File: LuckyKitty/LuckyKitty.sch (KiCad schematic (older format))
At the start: 19 parts

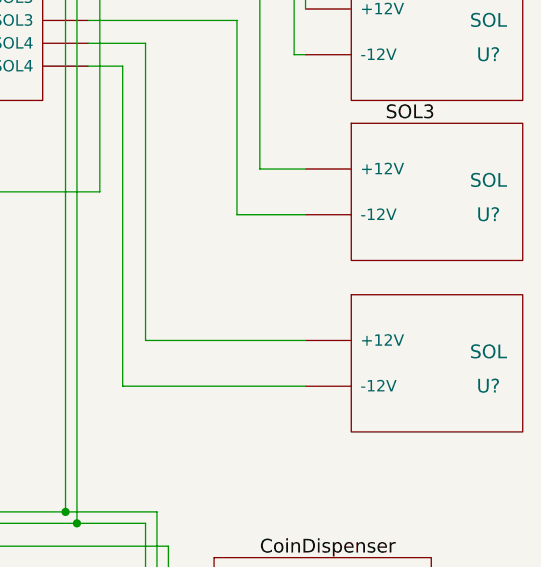
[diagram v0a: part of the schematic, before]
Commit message: Fixes a missing label on SOL4
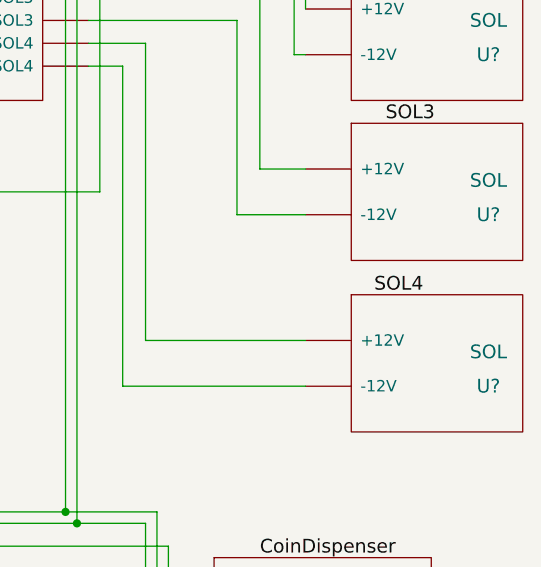
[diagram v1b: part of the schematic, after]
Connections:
- net at U?.~ (Vin): now also U?.~ (GND)
- net at U?.~ (SOL4): now also U?.~ (-12V); no longer U?.~ (-12V)
- new net: U?.~ (-12V), U?.~ (GND), U?.~ (Lin), U?.~ (SOL4)
- new net: U?.~ (GND), U?.~ (Lin), U?.~ (SOL4)
- new net: U?.~ (Din), U?.~ (Din), U?.~ (GND), U?.~ (GND), U?.~ (Lin), U?.~ (MOSI), U?.~ (MOSI), U?.~ (MOSI), U?.~ (SOL4), U?.~ (Vin)
- new net: U?.~ (Din), U?.~ (Din), U?.~ (Din), U?.~ (GND), U?.~ (MOSI), U?.~ (MOSI), U?.~ (MOSI), U?.~ (SOL4), U?.~ (Vin)
- new net: U?.0 (MOSI1), U?.~ (MOSI), U?.~ (MOSI), U?.~ (MOSI)
- new net: U?.1 (MISO1), U?.~ (MOSI), U?.~ (MOSI), U?.~ (MOSI)
- new net: U?.24, U?.~ (MOSI), U?.~ (MOSI), U?.~ (MOSI)
- new net: U?.32 (SCK1), U?.~ (MOSI), U?.~ (MOSI), U?.~ (MOSI)
- new net: U?.~ (Lin), U?.~ (Vin)
- new net: U?.~ (-12V), U?.~ (SOL4) (x4)
- now unconnected: U?.~ (-12V), U?.~ (Din), U?.~ (MOSI), U?.~ (MOSI), U?.~ (MOSI), U?.~ (MOSI), U?.~ (MOSI), U?.~ (MOSI), U?.~ (MOSI), U?.~ (MOSI), U?.~ (MOSI), U?.~ (MOSI), U?.~ (MOSI), U?.~ (MOSI), U?.~ (MOSI), U?.~ (MOSI), U?.~ (MOSI), U?.~ (MOSI), U?.~ (MOSI), U?.~ (MOSI)
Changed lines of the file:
@@
 LIBS:adafruit
 LIBS:Custom
+LIBS:LuckyKitty-cache
 EELAYER 25 0
 EELAYER END
@@
 Text Label 2750 650  0    60   ~ 0
 Examine
+Text Label 10350 4400 0    60   ~ 0
+SOL4
 $EndSCHEMATC

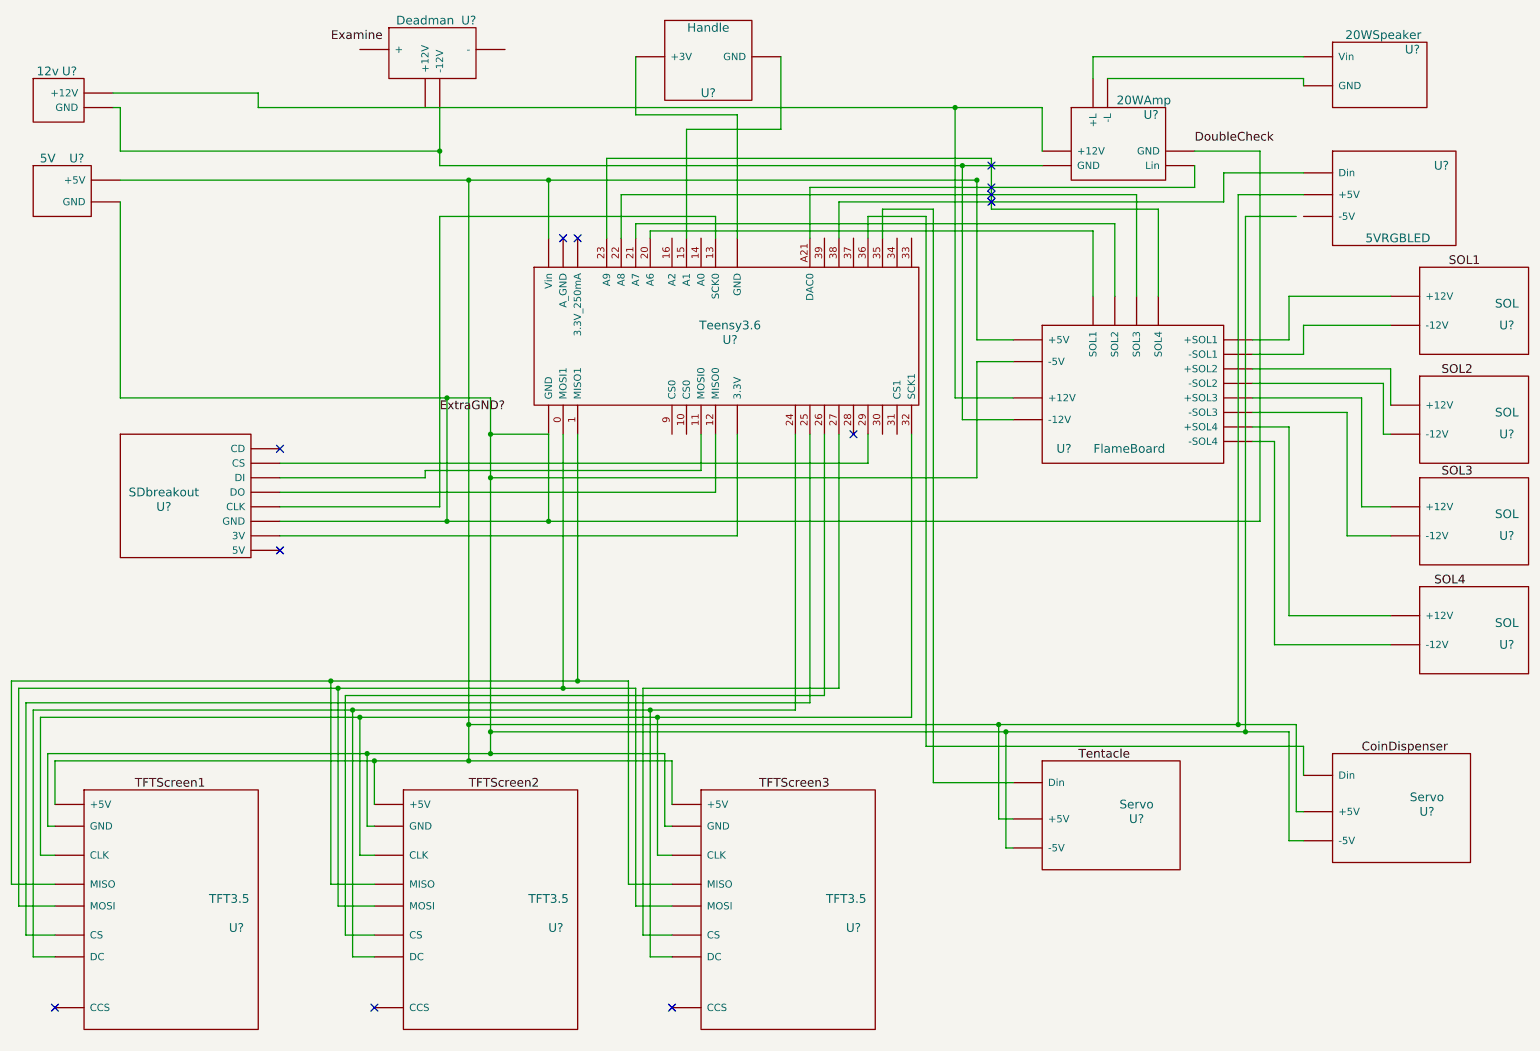
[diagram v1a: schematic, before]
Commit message: Adds safety lighting, fixes handle and sd breakout 5v, adds deadman init
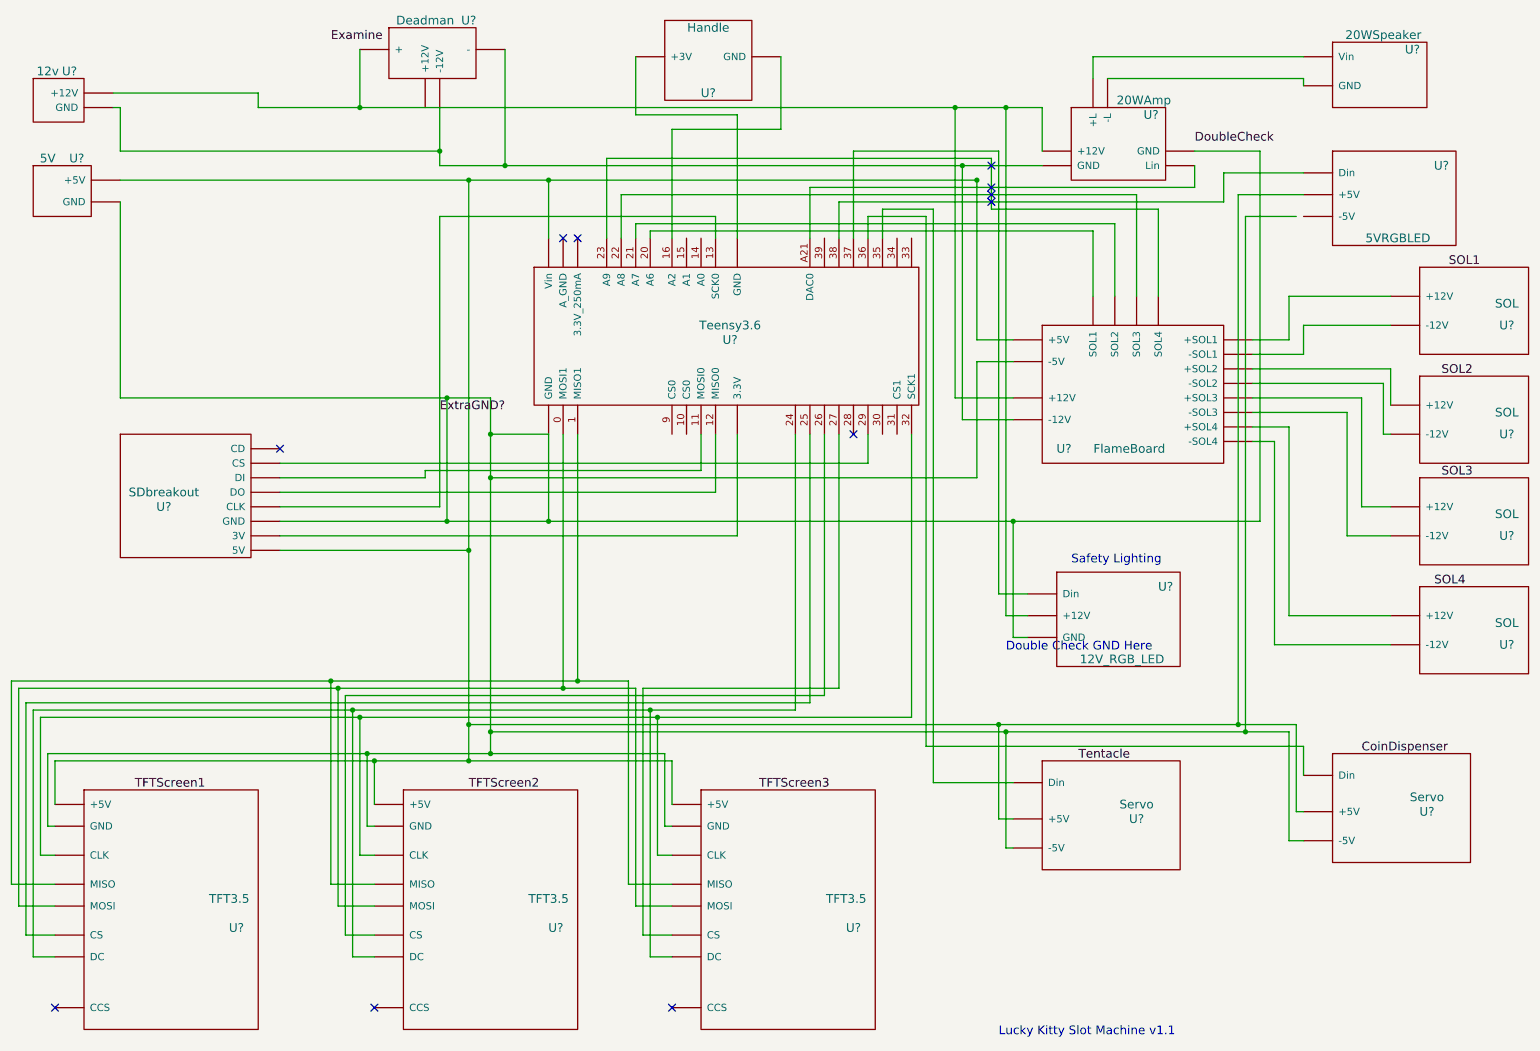
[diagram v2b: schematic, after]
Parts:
- added U?: 12V_RGB_LED, symbol 12V_RGB_LED
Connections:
- net at U?.15 (A1): no longer U?.~ (GND)
- net at U?.16 (A2): now also U?.~ (GND)
- net at U?.37: now also U?.~ (GND)
- net at U?.~ (Vin): now also U?.~ (GND)
- net at U?.~ (SOL4): now also U?.~ (-12V); no longer U?.~ (-12V)
- new net: U?.~ (-12V), U?.~ (GND), U?.~ (Lin), U?.~ (SOL4)
- new net: U?.~ (-12V), U?.~ (GND), U?.~ (GND), U?.~ (Lin), U?.~ (SOL4)
- new net: U?.~ (Din), U?.~ (Din), U?.~ (GND), U?.~ (GND), U?.~ (GND), U?.~ (Lin), U?.~ (MOSI), U?.~ (MOSI), U?.~ (MOSI), U?.~ (SOL4), U?.~ (Vin)
- new net: U?.~ (Din), U?.~ (Din), U?.~ (Din), U?.~ (GND), U?.~ (GND), U?.~ (MOSI), U?.~ (MOSI), U?.~ (MOSI), U?.~ (SOL4), U?.~ (Vin)
- new net: U?.0 (MOSI1), U?.~ (MOSI), U?.~ (MOSI), U?.~ (MOSI)
- new net: U?.1 (MISO1), U?.~ (MOSI), U?.~ (MOSI), U?.~ (MOSI)
- new net: U?.24, U?.~ (MOSI), U?.~ (MOSI), U?.~ (MOSI)
- new net: U?.32 (SCK1), U?.~ (MOSI), U?.~ (MOSI), U?.~ (MOSI)
- new net: U?.~ (Lin), U?.~ (Vin)
- new net: U?.~ (-12V), U?.~ (SOL4) (x4)
- now unconnected: U?.~ (-12V), U?.~ (Din), U?.~ (MOSI), U?.~ (MOSI), U?.~ (MOSI), U?.~ (MOSI), U?.~ (MOSI), U?.~ (MOSI), U?.~ (MOSI), U?.~ (MOSI), U?.~ (MOSI), U?.~ (MOSI), U?.~ (MOSI), U?.~ (MOSI), U?.~ (MOSI), U?.~ (MOSI), U?.~ (MOSI), U?.~ (MOSI), U?.~ (MOSI), U?.~ (MOSI)
- no-connect marks 12 -> 11
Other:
- note added: "Double Check GND Here"
- note added: "Lucky Kitty Slot Machine v1.1"
- note added: "Safety Lighting"
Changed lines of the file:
@@
 	2250 1100 7650 1100
-Wire Wire Line
-	5200 1250 5200 2000
 Wire Wire Line
 	8000 900  8000 750
@@
 	5550 1150 5550 2000
 Wire Wire Line
-	5200 1250 5850 1250
+	5100 1250 5850 1250
 Wire Wire Line
 	5850 1250 5850 750
@@
 	2400 3950 9150 3950
 Wire Wire Line
-	4250 3950 4250 3350
+	4250 3350 4250 3950
 Wire Wire Line
 	3550 3100 3550 3950
@@
 Connection ~ 3550 3100
 Wire Wire Line
-	6750 3350 6750 5300
-Wire Wire Line
-	6750 5300 750  5300
+	6750 5300 6750 3350
+Wire Wire Line
+	750  5300 6750 5300
 Wire Wire Line
 	750  5300 750  6250
@@
 Connection ~ 5000 5300
 Wire Wire Line
-	5950 3350 5950 5250
-Wire Wire Line
-	5950 5250 700  5250
+	5950 5250 5950 3350
+Wire Wire Line
+	700  5250 5950 5250
 Wire Wire Line
 	700  5250 700  6950
@@
 	4900 6800 5100 6800
 Wire Wire Line
-	4350 3350 4350 5100
+	4350 5100 4350 3350
 Wire Wire Line
 	600  5100 4850 5100
@@
 Connection ~ 4350 5100
 Wire Wire Line
-	4450 3350 4450 5050
+	4450 5050 4450 3350
 Wire Wire Line
 	550  5050 4800 5050
@@
 	7400 6200 7450 6200
 Connection ~ 7400 5400
-NoConn ~ 2400 4150
 NoConn ~ 850  7300
 NoConn ~ 3050 7300
@@
 Text Label 10350 4400 0    60   ~ 0
 SOL4
+Wire Wire Line
+	5100 2000 5100 1250
+Wire Wire Line
+	2950 700  2950 1100
+Connection ~ 2950 1100
+Wire Wire Line
+	3950 700  3950 1500
+Connection ~ 3950 1500
+Wire Wire Line
+	2400 4150 3700 4150
+Connection ~ 3700 4150
+$Comp
+L 12V_RGB_LED U?
+U 1 1 5AA6BADB
+P 8150 4600
+F 0 "U?" H 8500 4800 60  0000 C CNN
+F 1 "12V_RGB_LED" H 8200 4300 60  0000 C CNN
+F 2 "" H 8150 4600 60  0001 C CNN
+F 3 "" H 8150 4600 60  0001 C CNN
+	1    8150 4600
+	1    0    0    -1
+$EndComp
+Wire Wire Line
+	6350 2000 6350 1400
+Wire Wire Line
+	6350 1400 7350 1400
+Wire Wire Line
+	7350 1400 7350 4450
+Wire Wire Line
+	7350 4450 7550 4450
+Wire Wire Line
+	7400 1100 7400 4600
+Wire Wire Line
+	7400 4600 7550 4600
+Connection ~ 7400 1100
+Wire Wire Line
+	7550 4750 7450 4750
+Wire Wire Line
+	7450 4750 7450 3950
+Connection ~ 7450 3950
+Text Notes 7850 4250 0    60   ~ 0
+Safety Lighting
+Text Notes 7350 7500 0    60   ~ 0
+Lucky Kitty Slot Machine v1.1
+Text Notes 7400 4850 0    60   ~ 0
+Double Check GND Here
 $EndSCHEMATC
